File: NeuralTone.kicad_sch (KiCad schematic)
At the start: 84 parts, among them J1 5V@3A, J2 Guitar, J3 Headphone, J4 USB_A, J5 Line Out, J6 SD_Card, SW1 SW_Push, U1 MCP6022, U2 LDLN025M33, U3 LDLN025M33, U4 AP2151, U5 NAU8814YG, U6 USBLC6-2P6, Y1 DSB211SDN 26MHz

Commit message: increase voltage divider values
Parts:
- R10, R9: value 2k -> 10k
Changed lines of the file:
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@@
       (effects (font (size 1.27 1.27)) (justify right))
     )
-    (property "Value" "2k" (at 173.355 59.69 0)
+    (property "Value" "10k" (at 173.355 59.69 0)
       (effects (font (size 1.27 1.27)) (justify right))
     )
@@
       (effects (font (size 1.27 1.27)) (justify right))
     )
-    (property "Value" "2k" (at 173.355 69.85 0)
-      (effects (font (size 1.27 1.27)) (justify right))
-    )
+    (property "Value" "10k" (at 173.355 69.85 0)
+      (effects (font (size 1.27 1.27)) (justify right))
+    )

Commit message: assign initial footprints
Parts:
- C1, C10, C11, C12, C13, C14, C15, C16, C17, C19, C2, C20, C21, C22, C23, C24, C25, C27, C29, C30, C32, C4, C7, C8, C9: footprint (none) -> Capacitor_SMD:C_0805_2012Metric_Pad1.18x1.45mm_HandSolder
- C18, C26, C28, C3, C31, C5, C6: footprint (none) -> Capacitor_SMD:CP_Elec_4x5.7
- D1: footprint (none) -> Diode_SMD:D_SOD-123
- D2: footprint (none) -> Diode_SMD:D_SMF
- D3: footprint (none) -> Package_TO_SOT_SMD:SOT-23-3
- D4, D7: footprint (none) -> Package_TO_SOT_SMD:SOT-23-6_Handsoldering
- D5, D6: footprint (none) -> LED_SMD:LED_0805_2012Metric_Pad1.15x1.40mm_HandSolder
- F1: footprint (none) -> Fuse:Fuse_1812_4532Metric_Pad1.30x3.40mm_HandSolder
- J1: footprint (none) -> Connector_USB:USB_C_Receptacle_Amphenol_12401548E4-2A
- J2, J3, J5: footprint (none) -> Connector_Audio:Jack_6.35mm_Neutrik_NMJ6HFD4_Horizontal
- J4: footprint (none) -> Connector_USB:USB_A_Molex_67643_Horizontal
- J6: footprint (none) -> Connector_Card:microSD_HC_Hirose_DM3AT-SF-PEJM5
- R1, R10, R11, R12, R13, R14, R15, R16, R17, R18, R19, R2, R20, R21, R22, R23, R24, R25, R26, R27, R3, R4, R5, R6, R7, R8, R9: footprint (none) -> Resistor_SMD:R_0805_2012Metric_Pad1.20x1.40mm_HandSolder
- SW1: footprint (none) -> Button_Switch_SMD:SW_DIP_SPSTx01_Slide_6.7x4.1mm_W6.73mm_P2.54mm_LowProfile_JPin
- U1: footprint (none) -> Package_SO:SOIC-8_3.9x4.9mm_P1.27mm

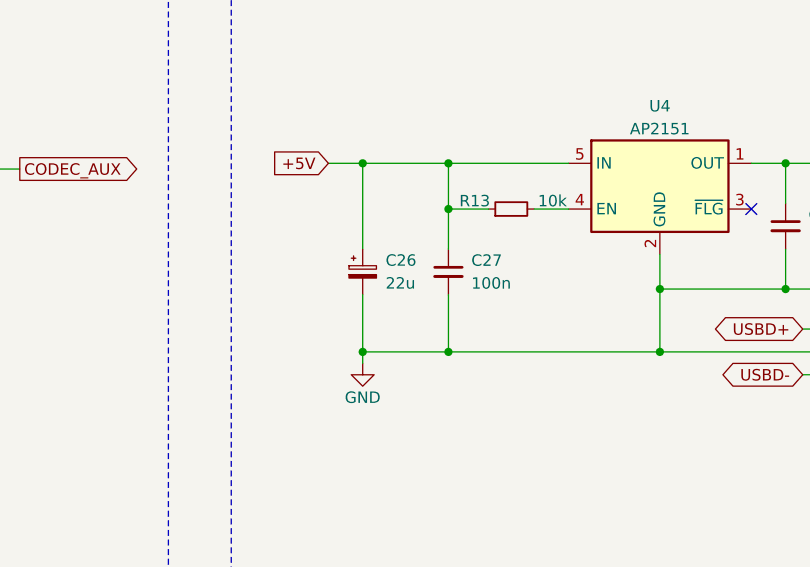
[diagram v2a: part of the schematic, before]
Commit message: change input cap for current limit switch
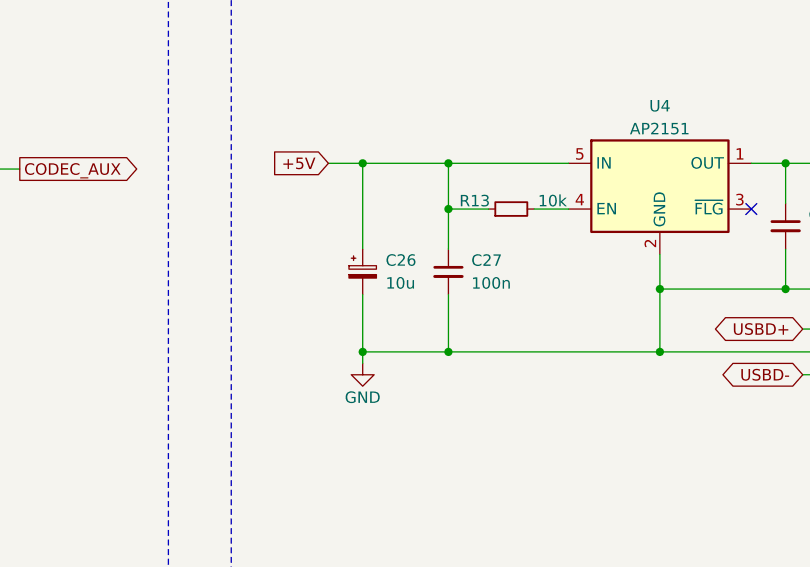
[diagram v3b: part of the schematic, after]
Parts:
- C26: value 22u -> 10u
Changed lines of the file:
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@@
       (effects (font (size 1.27 1.27)) (justify left))
     )
-    (property "Value" "22u" (at 302.26 59.055 0)
+    (property "Value" "10u" (at 302.26 59.055 0)
       (effects (font (size 1.27 1.27)) (justify left))
     )

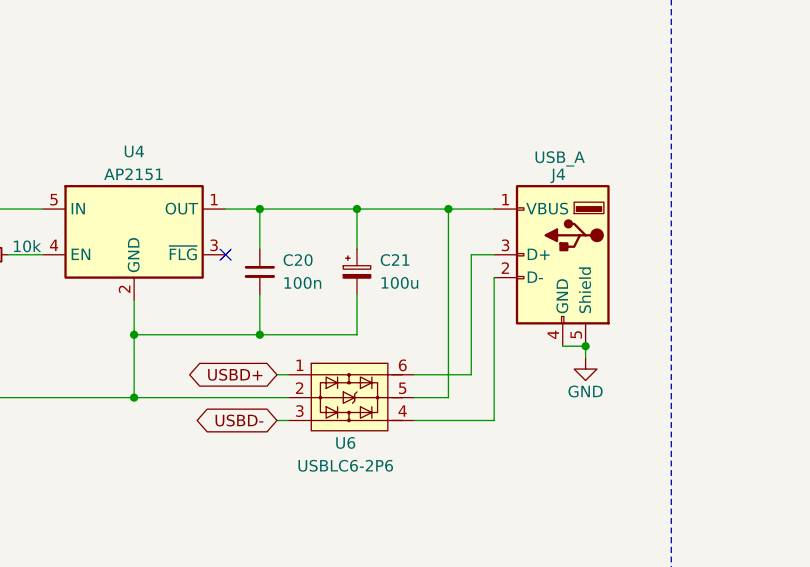
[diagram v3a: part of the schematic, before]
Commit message: change output cap for current limit switch
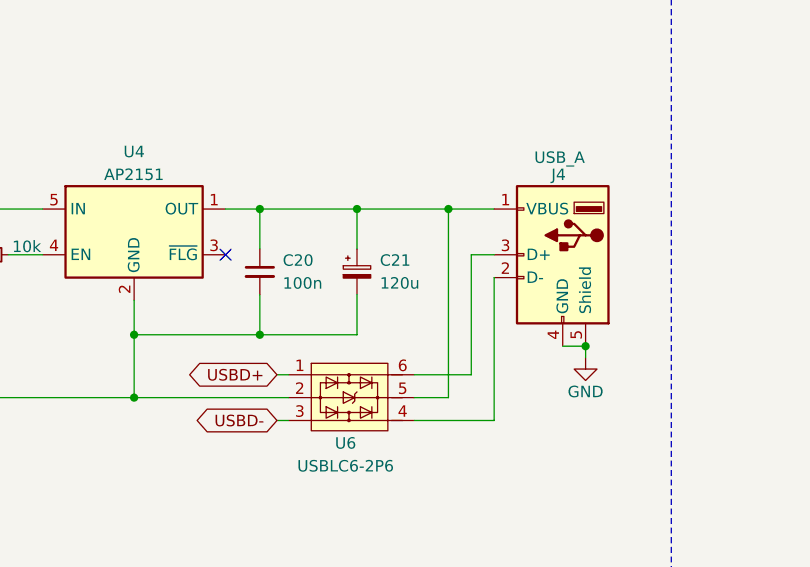
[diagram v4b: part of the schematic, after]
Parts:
- C21: value 100u -> 120u
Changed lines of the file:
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@@
       (effects (font (size 1.27 1.27)) (justify left))
     )
-    (property "Value" "100u" (at 360.045 53.975 0)
+    (property "Value" "120u" (at 360.045 53.975 0)
       (effects (font (size 1.27 1.27)) (justify left))
     )

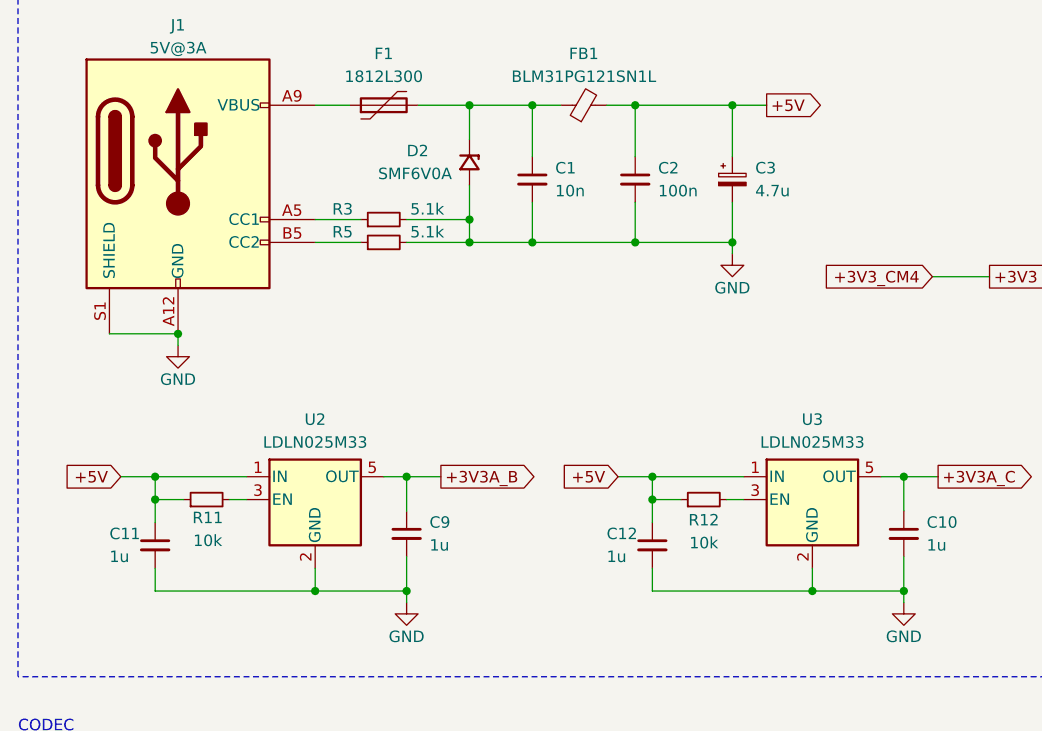
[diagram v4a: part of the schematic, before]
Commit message: footprint and annotation updates
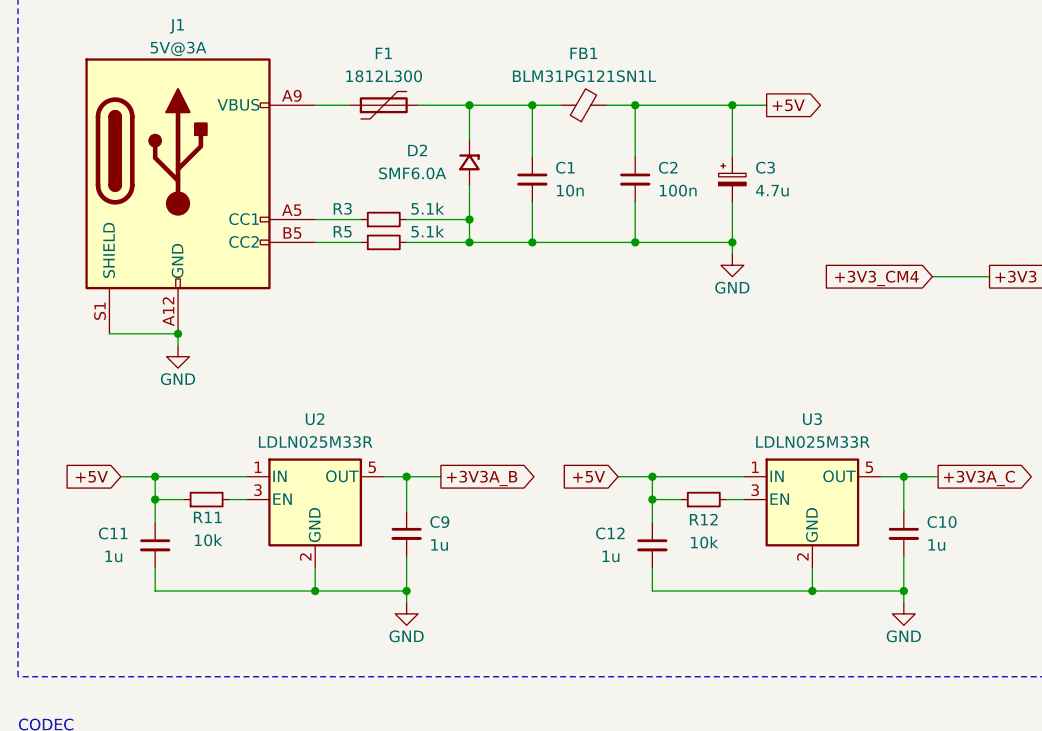
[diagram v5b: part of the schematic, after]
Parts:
- C21: footprint Capacitor_SMD:C_0805_2012Metric_Pad1.18x1.45mm_HandSolder -> Capacitor_SMD:CP_Elec_5x5.8
- D2: value SMF6V0A -> SMF6.0A; footprint Diode_SMD:D_SMF -> Diode_SMD:D_SOD-123F
- D3: footprint Package_TO_SOT_SMD:SOT-23-3 -> Package_TO_SOT_SMD:SOT-23_Handsoldering
- J2, J3, J5: footprint Connector_Audio:Jack_6.35mm_Neutrik_NMJ6HFD4_Horizontal -> Connector_Audio:Jack_6.35mm_Neutrik_NMJ6HCD2_Horizontal
- U2, U3: value LDLN025M33 -> LDLN025M33R; footprint Package_TO_SOT_SMD:SOT-23-5 -> Package_TO_SOT_SMD:SOT-23-5_HandSoldering
- U5: footprint NeuralTone:QFN-24_4X4_NUV-M -> Package_DFN_QFN:QFN-24-1EP_4x4mm_P0.5mm_EP2.6x2.6mm_ThermalVias
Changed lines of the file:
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@@
   (symbol (lib_id "Device:C_Small") (at 93.345 81.915 0) (unit 1)
     (in_bom yes) (on_board yes) (dnp no)
-    (property "Reference" "C12" (at 88.265 80.645 0)
-      (effects (font (size 1.27 1.27)) (justify left))
-    )
-    (property "Value" "1u" (at 88.265 83.185 0)
+    (property "Reference" "C12" (at 86.995 80.645 0)
+      (effects (font (size 1.27 1.27)) (justify left))
+    )
+    (property "Value" "1u" (at 87.63 83.185 0)
       (effects (font (size 1.27 1.27)) (justify left))
     )
@@
       (effects (font (size 1.27 1.27)) hide)
     )
-    (property "Datasheet" "" (at 83.312 181.864 90)
+    (property "Datasheet" "https://assets.nexperia.com/documents/data-sheet/PESD3V3S4UD.pdf" (at 83.312 181.864 90)
       (effects (font (size 1.27 1.27)) hide)
     )
@@
       (effects (font (size 1.27 1.27)))
     )
-    (property "Value" "LDLN025M33" (at 111.125 70.485 0)
-      (effects (font (size 1.27 1.27)))
-    )
-    (property "Footprint" "Package_TO_SOT_SMD:SOT-23-5" (at 111.125 68.58 0)
+    (property "Value" "LDLN025M33R" (at 111.125 70.485 0)
+      (effects (font (size 1.27 1.27)))
+    )
+    (property "Footprint" "Package_TO_SOT_SMD:SOT-23-5_HandSoldering" (at 111.125 68.58 0)
       (effects (font (size 1.27 1.27) italic) hide)
     )
@@
       (effects (font (size 1.27 1.27)) (justify left))
     )
-    (property "Value" "SMF6V0A" (at 62.865 40.64 90)
-      (effects (font (size 1.27 1.27)) (justify left))
-    )
-    (property "Footprint" "Diode_SMD:D_SMF" (at 73.025 39.37 90)
-      (effects (font (size 1.27 1.27)) hide)
-    )
-    (property "Datasheet" "" (at 73.025 39.37 90)
+    (property "Value" "SMF6.0A" (at 62.865 40.64 90)
+      (effects (font (size 1.27 1.27)) (justify left))
+    )
+    (property "Footprint" "Diode_SMD:D_SOD-123F" (at 73.025 39.37 90)
+      (effects (font (size 1.27 1.27)) hide)
+    )
+    (property "Datasheet" "https://www.littelfuse.com/media?resourcetype=datasheets&itemid=993a2ee6-c837-4498-91c6-aa64b06a6fb8&filename=littelfuse-tvs-diode-smf-datasheet" (at 73.025 39.37 90)
       (effects (font (size 1.27 1.27)) hide)
     )
@@
       (effects (font (size 1.27 1.27)))
     )
-    (property "Footprint" "Package_TO_SOT_SMD:SOT-23-3" (at 230.505 143.51 90)
-      (effects (font (size 1.27 1.27)) hide)
-    )
-    (property "Datasheet" "" (at 240.03 147.32 90)
+    (property "Footprint" "Package_TO_SOT_SMD:SOT-23_Handsoldering" (at 230.505 143.51 90)
+      (effects (font (size 1.27 1.27)) hide)
+    )
+    (property "Datasheet" "https://assets.nexperia.com/documents/data-sheet/PESD5V2S2UT.pdf" (at 240.03 147.32 90)
       (effects (font (size 1.27 1.27)) hide)
     )
@@
       (effects (font (size 1.27 1.27)) hide)
     )
-    (property "Datasheet" "" (at 65.913 254.381 90)
+    (property "Datasheet" "https://assets.nexperia.com/documents/data-sheet/PESD3V3S4UD.pdf" (at 65.913 254.381 90)
       (effects (font (size 1.27 1.27)) hide)
     )
@@
       (effects (font (size 1.27 1.27)) (justify right))
     )
-    (property "Footprint" "Connector_Audio:Jack_6.35mm_Neutrik_NMJ6HFD4_Horizontal" (at 159.385 43.815 0)
-      (effects (font (size 1.27 1.27)) hide)
-    )
-    (property "Datasheet" "~" (at 159.385 43.815 0)
+    (property "Footprint" "Connector_Audio:Jack_6.35mm_Neutrik_NMJ6HCD2_Horizontal" (at 159.385 43.815 0)
+      (effects (font (size 1.27 1.27)) hide)
+    )
+    (property "Datasheet" "https://datasheet.lcsc.com/lcsc/1912111437_HOOYA-PJ-609BA_C309277.pdf" (at 159.385 43.815 0)
       (effects (font (size 1.27 1.27)) hide)
     )
@@
       (effects (font (size 1.524 1.524)))
     )
-    (property "Footprint" "NeuralTone:QFN-24_4X4_NUV-M" (at 158.115 167.005 0)
+    (property "Footprint" "Package_DFN_QFN:QFN-24-1EP_4x4mm_P0.5mm_EP2.6x2.6mm_ThermalVias" (at 158.115 167.005 0)
       (effects (font (size 1.27 1.27) italic) hide)
     )
@@
       (effects (font (size 1.27 1.27)))
     )
-    (property "Footprint" "Connector_Audio:Jack_6.35mm_Neutrik_NMJ6HFD4_Horizontal" (at 257.81 158.115 0)
-      (effects (font (size 1.27 1.27)) hide)
-    )
-    (property "Datasheet" "~" (at 257.81 158.115 0)
+    (property "Footprint" "Connector_Audio:Jack_6.35mm_Neutrik_NMJ6HCD2_Horizontal" (at 257.81 158.115 0)
+      (effects (font (size 1.27 1.27)) hide)
+    )
+    (property "Datasheet" "https://datasheet.lcsc.com/lcsc/1912111437_HOOYA-PJ-609BA_C309277.pdf" (at 257.81 158.115 0)
       (effects (font (size 1.27 1.27)) hide)
     )
@@
       (effects (font (size 1.27 1.27)))
     )
-    (property "Footprint" "Connector_Audio:Jack_6.35mm_Neutrik_NMJ6HFD4_Horizontal" (at 257.81 123.19 0)
-      (effects (font (size 1.27 1.27)) hide)
-    )
-    (property "Datasheet" "~" (at 257.81 123.19 0)
+    (property "Footprint" "Connector_Audio:Jack_6.35mm_Neutrik_NMJ6HCD2_Horizontal" (at 257.81 123.19 0)
+      (effects (font (size 1.27 1.27)) hide)
+    )
+    (property "Datasheet" "https://datasheet.lcsc.com/lcsc/1912111437_HOOYA-PJ-609BA_C309277.pdf" (at 257.81 123.19 0)
       (effects (font (size 1.27 1.27)) hide)
     )
@@
   (symbol (lib_id "Device:C_Small") (at 38.1 81.915 0) (unit 1)
     (in_bom yes) (on_board yes) (dnp no)
-    (property "Reference" "C11" (at 33.02 80.645 0)
-      (effects (font (size 1.27 1.27)) (justify left))
-    )
-    (property "Value" "1u" (at 33.02 83.185 0)
+    (property "Reference" "C11" (at 31.75 80.645 0)
+      (effects (font (size 1.27 1.27)) (justify left))
+    )
+    (property "Value" "1u" (at 32.385 83.185 0)
       (effects (font (size 1.27 1.27)) (justify left))
     )
@@
       (effects (font (size 1.27 1.27)) (justify left))
     )
-    (property "Footprint" "Capacitor_SMD:C_0805_2012Metric_Pad1.18x1.45mm_HandSolder" (at 357.505 52.705 0)
+    (property "Footprint" "Capacitor_SMD:CP_Elec_5x5.8" (at 357.505 52.705 0)
       (effects (font (size 1.27 1.27)) hide)
     )
@@
       (effects (font (size 1.27 1.27)))
     )
-    (property "Value" "LDLN025M33" (at 55.88 70.485 0)
-      (effects (font (size 1.27 1.27)))
-    )
-    (property "Footprint" "Package_TO_SOT_SMD:SOT-23-5" (at 55.88 68.58 0)
+    (property "Value" "LDLN025M33R" (at 55.88 70.485 0)
+      (effects (font (size 1.27 1.27)))
+    )
+    (property "Footprint" "Package_TO_SOT_SMD:SOT-23-5_HandSoldering" (at 55.88 68.58 0)
       (effects (font (size 1.27 1.27) italic) hide)
     )

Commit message: footprint adjustments and fixes
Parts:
- removed J6: SD_Card, Connector_Card:microSD_HC_Hirose_DM3AT-SF-PEJM5, symbol Connector:SD_Card
- added J6: TF-01A, NeuralTone:TF-01A, symbol Connector:Micro_SD_Card
- J1: value 5V@3A -> 7010ASV; footprint Connector_USB:USB_C_Receptacle_Amphenol_12401548E4-2A -> Connector_USB:USB_C_Receptacle_G-Switch_GT-USB-7010ASV
- J4: value USB_A -> DS1095-WNR0; footprint Connector_USB:USB_A_Molex_67643_Horizontal -> Connector_USB:USB_A_CONNFLY_DS1095-WNR0
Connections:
- net +3V3: now also J6.4 (VDD); no longer C32.1
- net GND: now also J6.6 (VSS), J6.9 (SHIELD)
- net at D4.4 (K), R23.2: now also J6.3 (CMD)
- net at D4.1 (K), R20.2: now also J6.1 (DAT2)
- net at D4.3 (K), R22.2: now also J6.2 (DAT3/CD)
- net at D7.1 (K), R25.2: now also C32.1, J6.5 (CLK)
- net at D7.3 (K), R26.2: now also J6.7 (DAT0)
- net at D7.4 (K), R27.2: now also J6.8 (DAT1)
- no-connect marks 18 -> 16
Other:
- moved on the sheet: R25, R26, R27

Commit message: symbol fixes
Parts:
- J1: value 7010ASV -> Power Port (5V@3A)
- J4: value DS1095-WNR0 -> USB Port
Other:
- moved on the sheet: C13, C14, C15, C16, C17, C18, C19, C22, C23, C24, C25, C28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

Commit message: update elec cap footprints
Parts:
- C18, C26, C28, C3, C31, C5, C6: footprint Capacitor_SMD:CP_Elec_4x5.7 -> Capacitor_SMD:CP_Elec_4x5.4
- C21: footprint Capacitor_SMD:CP_Elec_5x5.8 -> Capacitor_SMD:CP_Elec_6.3x7.7
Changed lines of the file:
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@@
       (effects (font (size 1.27 1.27)))
     )
-    (property "Footprint" "Capacitor_SMD:CP_Elec_4x5.7" (at 241.935 46.355 0)
+    (property "Footprint" "Capacitor_SMD:CP_Elec_4x5.4" (at 241.935 46.355 0)
       (effects (font (size 1.27 1.27)) hide)
     )
@@
       (effects (font (size 1.27 1.27)) (justify left))
     )
-    (property "Footprint" "Capacitor_SMD:CP_Elec_4x5.7" (at 299.72 57.785 0)
+    (property "Footprint" "Capacitor_SMD:CP_Elec_4x5.4" (at 299.72 57.785 0)
       (effects (font (size 1.27 1.27)) hide)
     )
@@
       (effects (font (size 1.27 1.27)) (justify left))
     )
-    (property "Footprint" "Capacitor_SMD:CP_Elec_4x5.7" (at 161.925 68.58 0)
+    (property "Footprint" "Capacitor_SMD:CP_Elec_4x5.4" (at 161.925 68.58 0)
       (effects (font (size 1.27 1.27)) hide)
     )
@@
       (effects (font (size 1.27 1.27)) (justify left))
     )
-    (property "Footprint" "Capacitor_SMD:CP_Elec_4x5.7" (at 83.185 234.315 0)
+    (property "Footprint" "Capacitor_SMD:CP_Elec_4x5.4" (at 83.185 234.315 0)
       (effects (font (size 1.27 1.27)) hide)
     )
@@
       (effects (font (size 1.27 1.27)) (justify left))
     )
-    (property "Footprint" "Capacitor_SMD:CP_Elec_5x5.8" (at 357.505 52.705 0)
+    (property "Footprint" "Capacitor_SMD:CP_Elec_6.3x7.7" (at 357.505 52.705 0)
       (effects (font (size 1.27 1.27)) hide)
     )
@@
       (effects (font (size 1.27 1.27)))
     )
-    (property "Footprint" "Capacitor_SMD:CP_Elec_4x5.7" (at 224.79 153.67 0)
+    (property "Footprint" "Capacitor_SMD:CP_Elec_4x5.4" (at 224.79 153.67 0)
       (effects (font (size 1.27 1.27)) hide)
     )
@@
       (effects (font (size 1.27 1.27)) (justify left))
     )
-    (property "Footprint" "Capacitor_SMD:CP_Elec_4x5.7" (at 102.235 41.275 0)
+    (property "Footprint" "Capacitor_SMD:CP_Elec_4x5.4" (at 102.235 41.275 0)
       (effects (font (size 1.27 1.27)) hide)
     )
@@
       (effects (font (size 1.27 1.27)))
     )
-    (property "Footprint" "Capacitor_SMD:CP_Elec_4x5.7" (at 224.79 128.905 0)
-      (effects (font (size 1.27 1.27)) hide)
-    )
+    (property "Footprint" "Capacitor_SMD:CP_Elec_4x5.4" (at 224.79 128.905 0)
+      (effects (font (size 1.27 1.27)) hide)
+    )
